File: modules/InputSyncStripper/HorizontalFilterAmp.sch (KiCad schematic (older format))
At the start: 10 parts

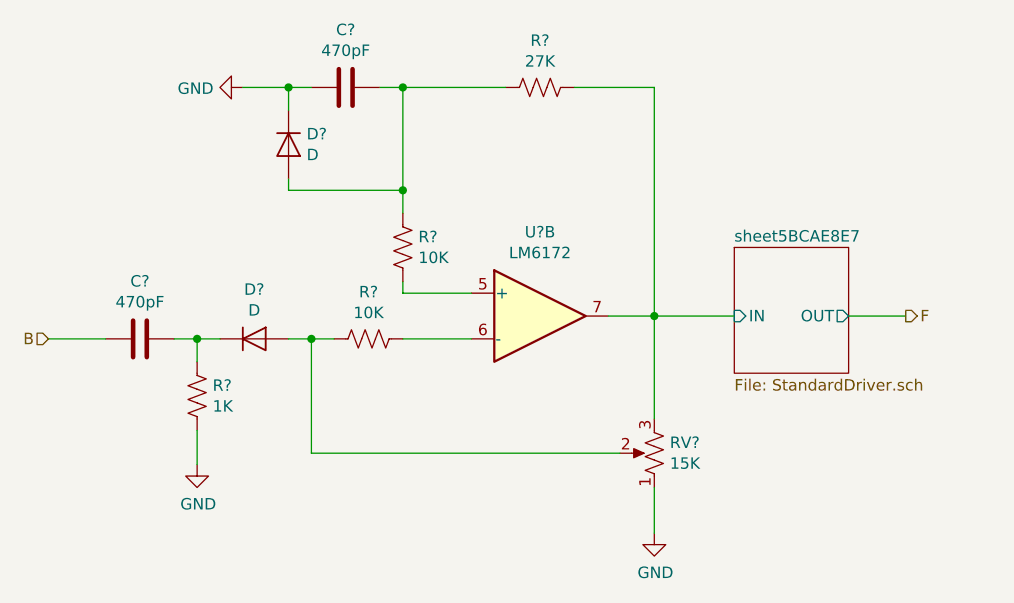
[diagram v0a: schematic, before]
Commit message: fix some ERC issues; assign symbols
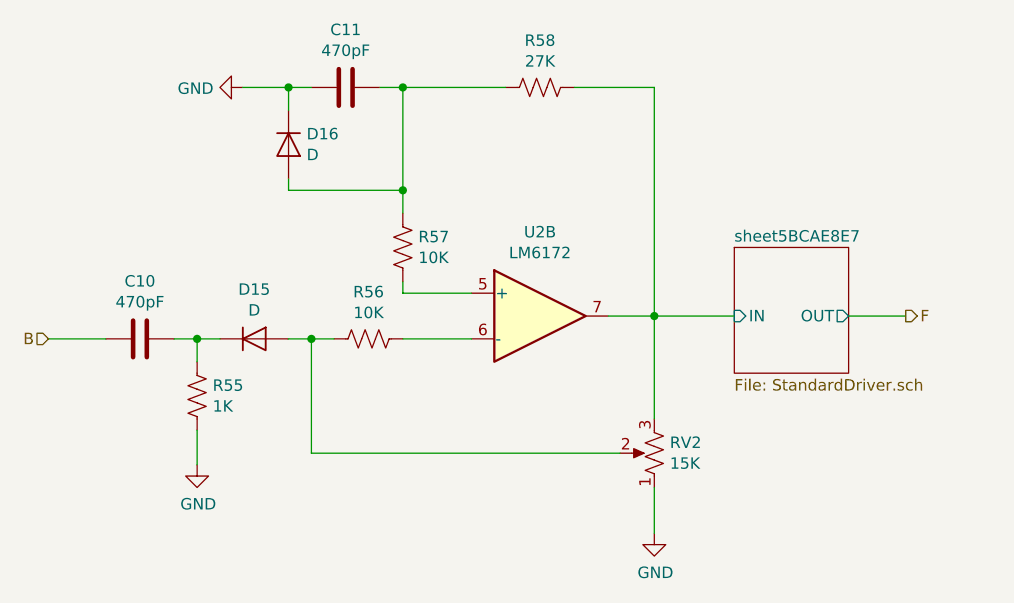
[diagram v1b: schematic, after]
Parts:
- gave numbers to parts that had none: 10
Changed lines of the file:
@@
 EESchema Schematic File Version 4
-LIBS:SIP-cache
+LIBS:InputSyncStripper-cache
 EELAYER 26 0
 EELAYER END
@@
 $EndDescr
 $Comp
-L Amplifier_Operational:LM6172 U?
+L Amplifier_Operational:LM6172 U2
 U 2 1 5BCAE849
 P 4550 3600
-F 0 "U?" H 4550 3967 50  0000 C CNN
+F 0 "U2" H 4550 3967 50  0000 C CNN
 F 1 "LM6172" H 4550 3876 50  0000 C CNN
 F 2 "" H 4550 3600 50  0001 C CNN
@@
 $EndSheet
 $Comp
-L Device:R_US R?
+L Device:R_US R58
 U 1 1 5BCAE90D
 P 4550 2600
-F 0 "R?" V 4345 2600 50  0000 C CNN
+F 0 "R58" V 4345 2600 50  0000 C CNN
 F 1 "27K" V 4436 2600 50  0000 C CNN
 F 2 "" V 4590 2590 50  0001 C CNN
@@
 $EndComp
 $Comp
-L Device:R_US R?
+L Device:R_US R57
 U 1 1 5BCAE970
 P 3950 3300
-F 0 "R?" H 4018 3346 50  0000 L CNN
+F 0 "R57" H 4018 3346 50  0000 L CNN
 F 1 "10K" H 4018 3255 50  0000 L CNN
 F 2 "" V 3990 3290 50  0001 C CNN
@@
 $EndComp
 $Comp
-L Device:C C?
+L Device:C C11
 U 1 1 5BCAE9EF
 P 3700 2600
-F 0 "C?" V 3448 2600 50  0000 C CNN
+F 0 "C11" V 3448 2600 50  0000 C CNN
 F 1 "470pF" V 3539 2600 50  0000 C CNN
 F 2 "" H 3738 2450 50  0001 C CNN
@@
 $EndComp
 $Comp
-L Device:D D?
+L Device:D D16
 U 1 1 5BCAEA71
 P 3450 2850
-F 0 "D?" V 3404 2929 50  0000 L CNN
+F 0 "D16" V 3404 2929 50  0000 L CNN
 F 1 "D" V 3495 2929 50  0000 L CNN
 F 2 "" H 3450 2850 50  0001 C CNN
@@
 	3950 2600 4400 2600
 $Comp
-L power:GND #PWR?
+L power:GND #PWR027
 U 1 1 5BCAED5B
 P 3250 2600
-F 0 "#PWR?" H 3250 2350 50  0001 C CNN
+F 0 "#PWR027" H 3250 2350 50  0001 C CNN
 F 1 "GND" V 3255 2472 50  0000 R CNN
 F 2 "" H 3250 2600 50  0001 C CNN
@@
 Connection ~ 3450 2600
 $Comp
-L Device:R_POT_US RV?
+L Device:R_POT_US RV2
 U 1 1 5BCAEE7B
 P 5050 4200
-F 0 "RV?" H 4982 4154 50  0000 R CNN
+F 0 "RV2" H 4982 4154 50  0000 R CNN
 F 1 "15K" H 4982 4245 50  0000 R CNN
 F 2 "" H 5050 4200 50  0001 C CNN
@@
 $EndComp
 $Comp
-L power:GND #PWR?
+L power:GND #PWR028
 U 1 1 5BCAEF3F
 P 5050 4550
-F 0 "#PWR?" H 5050 4300 50  0001 C CNN
+F 0 "#PWR028" H 5050 4300 50  0001 C CNN
 F 1 "GND" H 5055 4377 50  0000 C CNN
 F 2 "" H 5050 4550 50  0001 C CNN
@@
 	5050 4050 5050 3600
 $Comp
-L Device:R_US R?
+L Device:R_US R56
 U 1 1 5BCAF182
 P 3800 3700
-F 0 "R?" V 3595 3700 50  0000 C CNN
+F 0 "R56" V 3595 3700 50  0000 C CNN
 F 1 "10K" V 3686 3700 50  0000 C CNN
 F 2 "" V 3840 3690 50  0001 C CNN
@@
 	3950 3700 4250 3700
 $Comp
-L Device:D D?
+L Device:D D15
 U 1 1 5BCAF325
 P 3300 3700
-F 0 "D?" H 3300 3916 50  0000 C CNN
+F 0 "D15" H 3300 3916 50  0000 C CNN
 F 1 "D" H 3300 3825 50  0000 C CNN
 F 2 "" H 3300 3700 50  0001 C CNN
@@
 $EndComp
 $Comp
-L Device:C C?
+L Device:C C10
 U 1 1 5BCAF39E
 P 2800 3700
-F 0 "C?" V 2548 3700 50  0000 C CNN
+F 0 "C10" V 2548 3700 50  0000 C CNN
 F 1 "470pF" V 2639 3700 50  0000 C CNN
 F 2 "" H 2838 3550 50  0001 C CNN
@@
 $EndComp
 $Comp
-L Device:R_US R?
+L Device:R_US R55
 U 1 1 5BCAF432
 P 3050 3950
-F 0 "R?" H 3118 3996 50  0000 L CNN
+F 0 "R55" H 3118 3996 50  0000 L CNN
 F 1 "1K" H 3118 3905 50  0000 L CNN
 F 2 "" V 3090 3940 50  0001 C CNN
@@
 	3050 3700 3150 3700
 $Comp
-L power:GND #PWR?
+L power:GND #PWR026
 U 1 1 5BCAFCCD
 P 3050 4250
-F 0 "#PWR?" H 3050 4000 50  0001 C CNN
+F 0 "#PWR026" H 3050 4000 50  0001 C CNN
 F 1 "GND" H 3055 4077 50  0000 C CNN
 F 2 "" H 3050 4250 50  0001 C CNN

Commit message: added power pins for opamps and tied inputs of unused amp
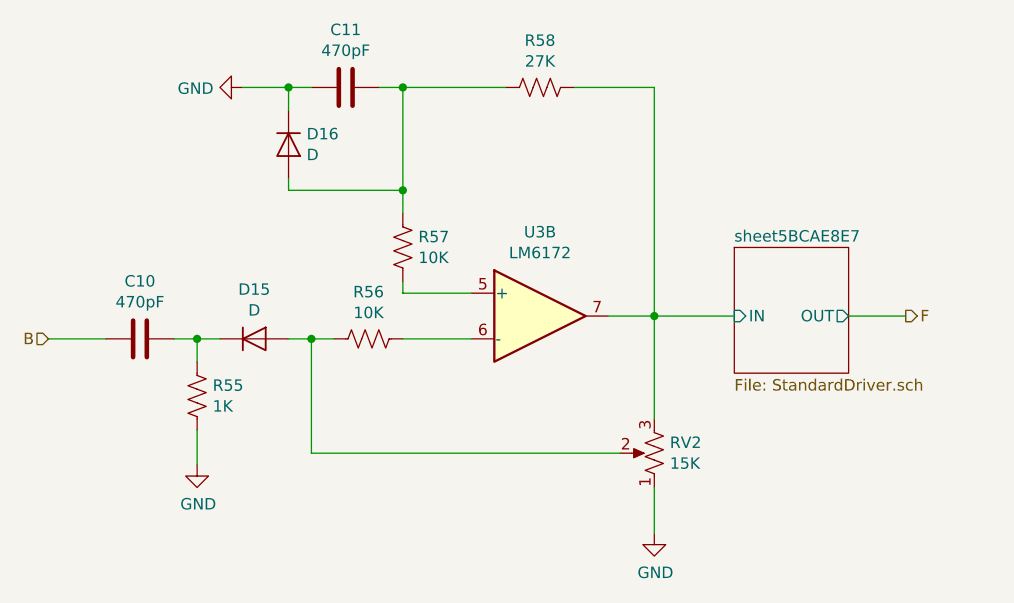
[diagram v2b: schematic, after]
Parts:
- renumbered U2 to U3
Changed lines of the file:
@@
 $EndDescr
 $Comp
-L Amplifier_Operational:LM6172 U2
+L Amplifier_Operational:LM6172 U3
 U 2 1 5BCAE849
 P 4550 3600
-F 0 "U2" H 4550 3967 50  0000 C CNN
+F 0 "U3" H 4550 3967 50  0000 C CNN
 F 1 "LM6172" H 4550 3876 50  0000 C CNN
 F 2 "" H 4550 3600 50  0001 C CNN

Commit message: Find and fix missing values
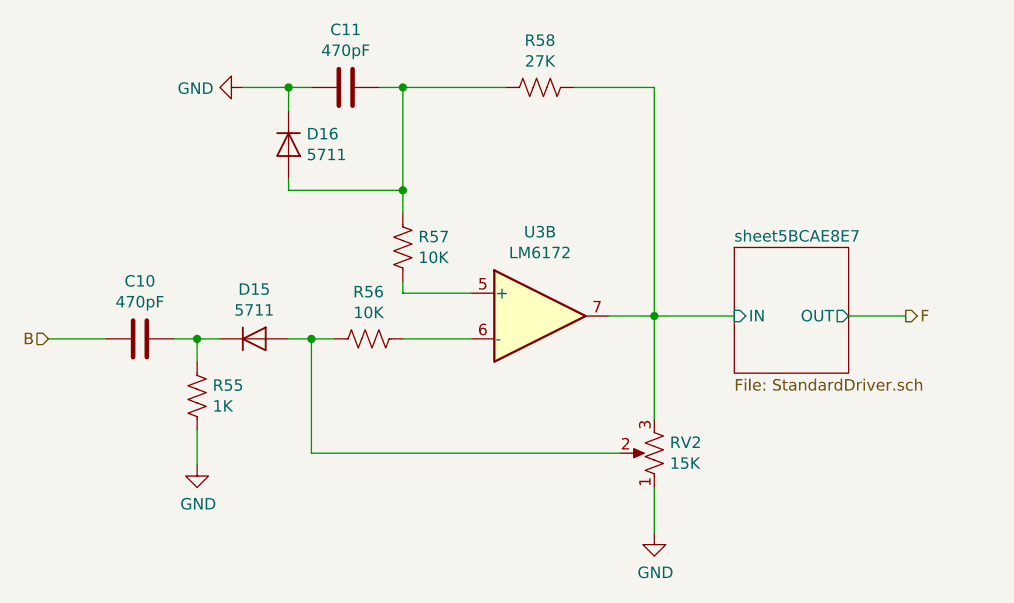
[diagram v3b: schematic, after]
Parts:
- D15, D16: value D -> 5711
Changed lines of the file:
@@
 P 3450 2850
 F 0 "D16" V 3404 2929 50  0000 L CNN
-F 1 "D" V 3495 2929 50  0000 L CNN
+F 1 "5711" V 3495 2929 50  0000 L CNN
 F 2 "" H 3450 2850 50  0001 C CNN
 F 3 "~" H 3450 2850 50  0001 C CNN
@@
 P 3300 3700
 F 0 "D15" H 3300 3916 50  0000 C CNN
-F 1 "D" H 3300 3825 50  0000 C CNN
+F 1 "5711" H 3300 3825 50  0000 C CNN
 F 2 "" H 3300 3700 50  0001 C CNN
 F 3 "~" H 3300 3700 50  0001 C CNN

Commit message: building out footprints/BOM
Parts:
- C10, C11: footprint (none) -> Capacitor_SMD:C_0805_2012Metric_Pad1.15x1.40mm_HandSolder
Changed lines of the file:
@@
 F 0 "C11" V 3448 2600 50  0000 C CNN
 F 1 "470pF" V 3539 2600 50  0000 C CNN
-F 2 "" H 3738 2450 50  0001 C CNN
+F 2 "Capacitor_SMD:C_0805_2012Metric_Pad1.15x1.40mm_HandSolder" H 3738 2450 50  0001 C CNN
 F 3 "~" H 3700 2600 50  0001 C CNN
 	1    3700 2600
@@
 F 0 "C10" V 2548 3700 50  0000 C CNN
 F 1 "470pF" V 2639 3700 50  0000 C CNN
-F 2 "" H 2838 3550 50  0001 C CNN
+F 2 "Capacitor_SMD:C_0805_2012Metric_Pad1.15x1.40mm_HandSolder" H 2838 3550 50  0001 C CNN
 F 3 "~" H 2800 3700 50  0001 C CNN
 	1    2800 3700
